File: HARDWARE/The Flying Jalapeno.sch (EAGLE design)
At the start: 97 parts, among them Q1 BSS138, 200mA/50V, Q2 MMBT2222A, Q3 NDP6020P, Q4 MMBT2222A, Q5 NDP6020P, Q6 BSS138, 200mA/50V, U1 ATMEGA2560AU, U2 LM1117, U3 LM1117, U4 LM1117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

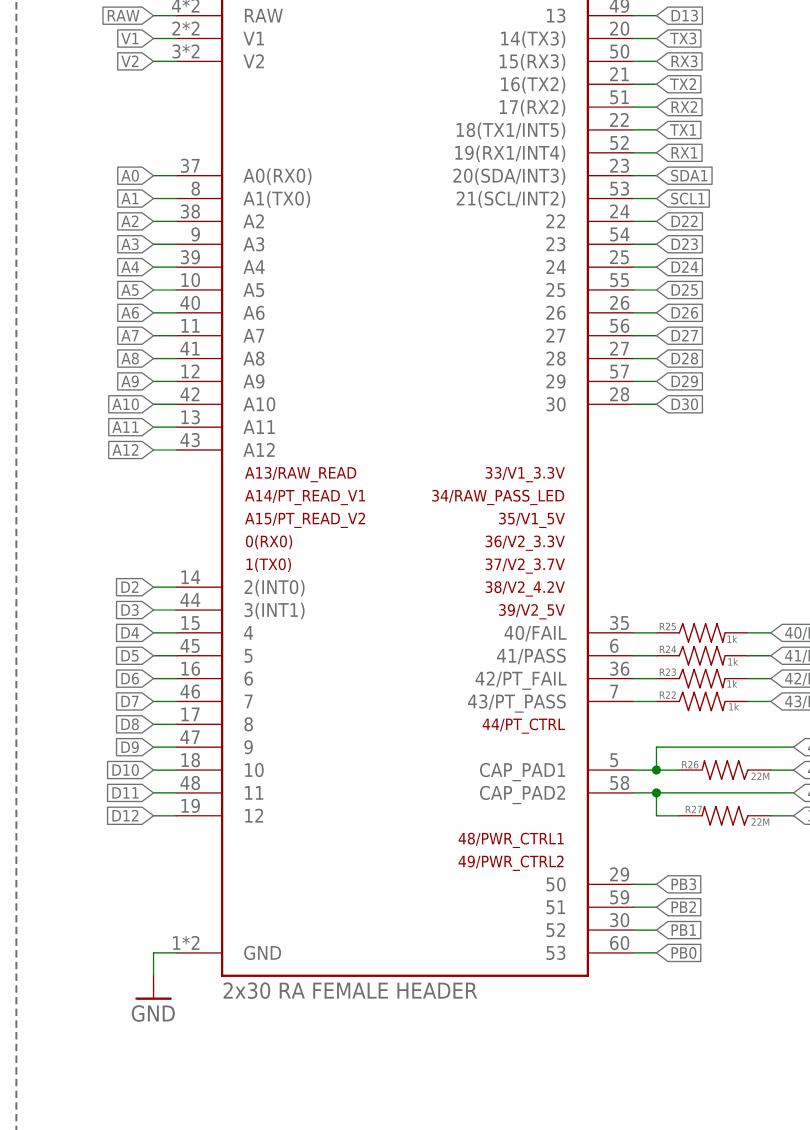
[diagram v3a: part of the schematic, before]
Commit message: Updated FJ device - symbol and package
Symbol pins are now correctly named A0 and A1, they used to have A0/TX0
and A1/RX0, which is incorrect and left over from the mega pro designs.

Also, with this update to the device came a small update to the package.
Only thing effected was the drill hits for the brackets are now the
correct "tighter" size of 0.11".
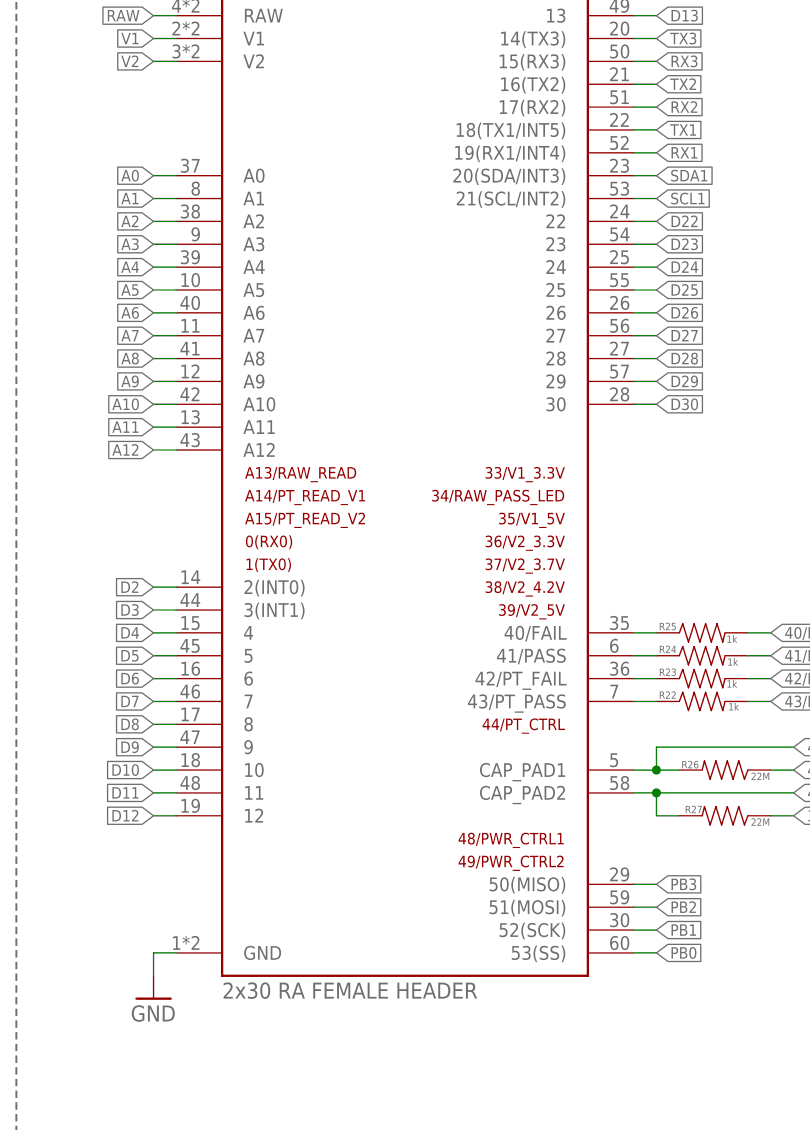
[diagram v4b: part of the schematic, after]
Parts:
- JP4: device Testing:FLYING_JALAPENO_V2FEMALE -> Testing:FLYING_JALAPENO_V3FEMALE
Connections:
- net A0: now also JP4.A0; no longer JP4.A0(RX0)
- net A1: now also JP4.A1; no longer JP4.A1(TX0)
- net PB0: now also JP4.53(SS); no longer JP4.53
- net PB1: now also JP4.52(SCK); no longer JP4.52
- net PB2: now also JP4.51(MOSI); no longer JP4.51
- net PB3: now also JP4.50(MISO); no longer JP4.50
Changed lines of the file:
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@@
 <part name="P+7" library="SparkFun" deviceset="3.3V" device="" value="VCC"/>
 <part name="P+9" library="SparkFun" deviceset="3.3V" device="" value="VCC"/>
-<part name="JP4" library="Testing" deviceset="FLYING_JALAPENO_V2" device="FEMALE" value="2x30 RA FEMALE HEADER"/>
+<part name="JP4" library="Testing" deviceset="FLYING_JALAPENO_V3" device="FEMALE" value="2x30 RA FEMALE HEADER"/>
 <part name="GND54" library="SparkFun" deviceset="GND" device=""/>
 <part name="STANDOFF2" library="SparkFun-Electromechanical" deviceset="STAND-OFF" device="TIGHT"/>
@@
 <segment>
 <wire x1="345.44" y1="213.36" x2="342.9" y2="213.36" width="0.1524" layer="91"/>
-<pinref part="JP4" gate="G$1" pin="A1(TX0)"/>
+<pinref part="JP4" gate="G$1" pin="A1"/>
 <label x="342.9" y="213.36" size="1.27" layer="95" rot="R180" xref="yes"/>
 </segment>
@@
 <segment>
 <wire x1="345.44" y1="215.9" x2="342.9" y2="215.9" width="0.1524" layer="91"/>
-<pinref part="JP4" gate="G$1" pin="A0(RX0)"/>
+<pinref part="JP4" gate="G$1" pin="A0"/>
 <label x="342.9" y="215.9" size="1.27" layer="95" rot="R180" xref="yes"/>
 </segment>
@@
 <segment>
 <wire x1="396.24" y1="129.54" x2="398.78" y2="129.54" width="0.1524" layer="91"/>
-<pinref part="JP4" gate="G$1" pin="53"/>
+<pinref part="JP4" gate="G$1" pin="53(SS)"/>
 <label x="398.78" y="129.54" size="1.27" layer="95" xref="yes"/>
 </segment>
@@
 <segment>
 <wire x1="396.24" y1="132.08" x2="398.78" y2="132.08" width="0.1524" layer="91"/>
-<pinref part="JP4" gate="G$1" pin="52"/>
+<pinref part="JP4" gate="G$1" pin="52(SCK)"/>
 <label x="398.78" y="132.08" size="1.27" layer="95" xref="yes"/>
 </segment>
@@
 <segment>
 <wire x1="396.24" y1="134.62" x2="398.78" y2="134.62" width="0.1524" layer="91"/>
-<pinref part="JP4" gate="G$1" pin="51"/>
+<pinref part="JP4" gate="G$1" pin="51(MOSI)"/>
 <label x="398.78" y="134.62" size="1.27" layer="95" xref="yes"/>
 </segment>
@@
 <segment>
 <wire x1="396.24" y1="137.16" x2="398.78" y2="137.16" width="0.1524" layer="91"/>
-<pinref part="JP4" gate="G$1" pin="50"/>
+<pinref part="JP4" gate="G$1" pin="50(MISO)"/>
 <label x="398.78" y="137.16" size="1.27" layer="95" xref="yes"/>
 </segment>
